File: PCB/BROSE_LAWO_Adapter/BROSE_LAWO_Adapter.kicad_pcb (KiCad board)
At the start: 2 copper layers, 37 x 89.5 mm, 7 parts, among them J1 LAWO Controller, J2 BROSE, J3 24V

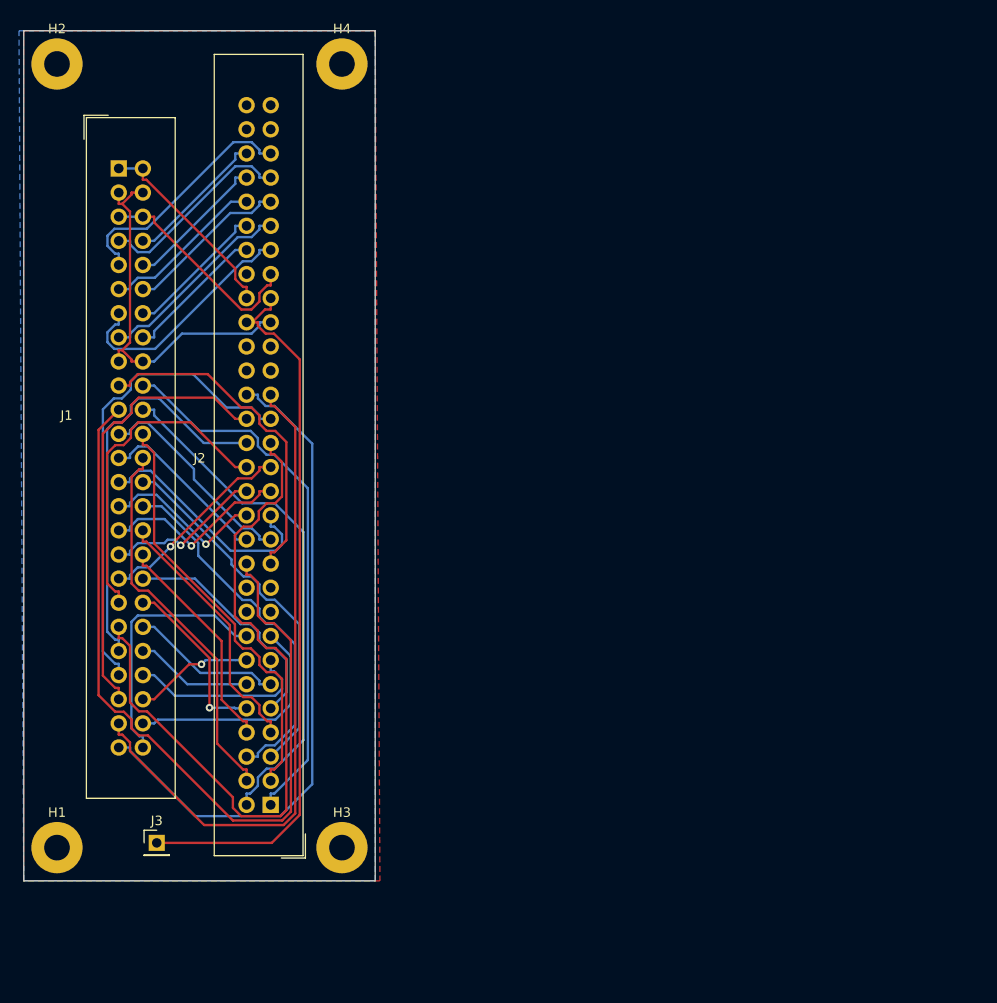
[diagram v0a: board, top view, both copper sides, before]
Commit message: update BROSE_LAWO Adapter PCB
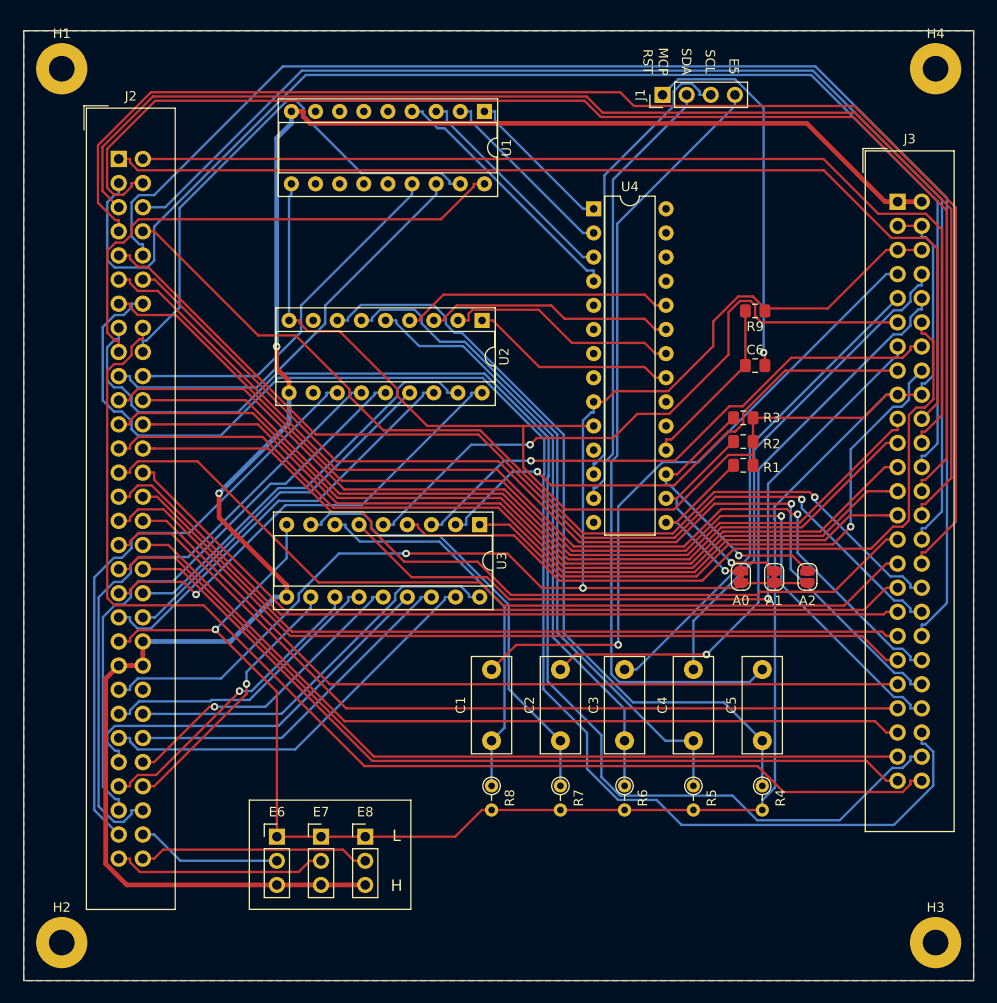
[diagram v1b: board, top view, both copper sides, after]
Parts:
- added C1: 330n, Capacitor_THT:C_Rect_L10.0mm_W4.0mm_P7.50mm_MKS4, F.Cu at (62.2, 87.8)
- added C2: 330n, Capacitor_THT:C_Rect_L10.0mm_W4.0mm_P7.50mm_MKS4, F.Cu at (69.5, 87.8)
- added C3: 330n, Capacitor_THT:C_Rect_L10.0mm_W4.0mm_P7.50mm_MKS4, F.Cu at (76.2, 87.8)
- added C4: 330n, Capacitor_THT:C_Rect_L10.0mm_W4.0mm_P7.50mm_MKS4, F.Cu at (83.5, 87.8)
- added C5: 330n, Capacitor_THT:C_Rect_L10.0mm_W4.0mm_P7.50mm_MKS4, F.Cu at (90.8, 87.8)
- added C6: 100n, Capacitor_SMD:C_0805_2012Metric_Pad1.15x1.40mm_HandSolder, F.Cu at (90.0, 48.2)
- added JP1: E6, Connector_PinHeader_2.54mm:PinHeader_1x03_P2.54mm_Vertical, F.Cu at (39.6, 97.8)
- added JP2: E7, Connector_PinHeader_2.54mm:PinHeader_1x03_P2.54mm_Vertical, F.Cu at (44.3, 97.8)
- added JP3: E8, Connector_PinHeader_2.54mm:PinHeader_1x03_P2.54mm_Vertical, F.Cu at (49.0, 97.8)
- added JP4: A0, Jumper:SolderJumper-2_P1.3mm_Bridged_RoundedPad1.0x1.5mm, F.Cu at (88.5, 70.5)
- added JP5: A1, Jumper:SolderJumper-2_P1.3mm_Bridged_RoundedPad1.0x1.5mm, F.Cu at (92.0, 70.5)
- added JP6: A2, Jumper:SolderJumper-2_P1.3mm_Open_RoundedPad1.0x1.5mm, F.Cu at (95.5, 70.5)
- added R1: 10k, Resistor_SMD:R_0805_2012Metric_Pad1.15x1.40mm_HandSolder, F.Cu at (88.8, 58.8)
- added R2: 10k, Resistor_SMD:R_0805_2012Metric_Pad1.15x1.40mm_HandSolder, F.Cu at (88.8, 56.2)
- added R3: 10k, Resistor_SMD:R_0805_2012Metric_Pad1.15x1.40mm_HandSolder, F.Cu at (88.8, 53.8)
- added R4: 15k, Resistor_THT:R_Axial_DIN0204_L3.6mm_D1.6mm_P2.54mm_Vertical, F.Cu at (90.8, 92.5)
- added R5: 15k, Resistor_THT:R_Axial_DIN0204_L3.6mm_D1.6mm_P2.54mm_Vertical, F.Cu at (83.5, 92.5)
- added R6: 15k, Resistor_THT:R_Axial_DIN0204_L3.6mm_D1.6mm_P2.54mm_Vertical, F.Cu at (76.2, 92.5)
- added R7: 15k, Resistor_THT:R_Axial_DIN0204_L3.6mm_D1.6mm_P2.54mm_Vertical, F.Cu at (69.5, 92.5)
- added R8: 15k, Resistor_THT:R_Axial_DIN0204_L3.6mm_D1.6mm_P2.54mm_Vertical, F.Cu at (62.2, 92.5)
- added R9: 10k, Resistor_SMD:R_0805_2012Metric_Pad1.15x1.40mm_HandSolder, F.Cu at (90.0, 42.5)
- added U1: UDN2981A / TBD62783, Package_DIP:DIP-18_W7.62mm_Socket, F.Cu at (61.5, 21.5)
- added U2: ULN2803A, Package_DIP:DIP-18_W7.62mm_Socket, F.Cu at (61.2, 43.5)
- added U3: ULN2803A, Package_DIP:DIP-18_W7.62mm_Socket, F.Cu at (61.0, 65.0)
- added U4: MCP23017_SP, Package_DIP:DIP-28_W7.62mm, F.Cu at (73.0, 31.8)
- J1: value LAWO Controller -> Conn_01x04; footprint Connector_IDC:IDC-Header_2x25_P2.54mm_Vertical -> Connector_PinHeader_2.54mm:PinHeader_1x04_P2.54mm_Vertical
- J3: value 24V -> LAWO Controller; footprint Connector_PinHeader_2.54mm:PinHeader_1x01_P2.54mm_Vertical -> Connector_IDC:IDC-Header_2x25_P2.54mm_Vertical
- moved J3 103.2 mm to (105.0, 31.0)
- moved H2 92.5 mm to (17.0, 109.0)
- moved H1 82.0 mm to (17.0, 17.0)
- moved J2 69.9 mm to (23.0, 26.5), turned to 0 degrees
- moved H3 63.3 mm to (109.0, 109.0)
- moved H4 62.5 mm to (109.0, 17.0)
- moved J1 57.8 mm to (80.2, 19.8), turned to 90 degrees
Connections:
- J1 pad 1: /VS -> /MCP_RESET
- J1 pad 2: /VS -> /SDA
- J1 pad 3: GND -> /SCL
- J1 pad 4: GND -> /E5
- J2 pad 17: Net-(J2-Pad17) -> /Y_R17
- J2 pad 18: Net-(J2-Pad18) -> /Y_R18
- J2 pad 19: Net-(J2-Pad19) -> /Y_R19
- J2 pad 20: Net-(J2-Pad20) -> /Y_R20
- J2 pad 37: Net-(J2-Pad37) -> /B_R17
- J2 pad 38: Net-(J2-Pad38) -> /B_R18
- J2 pad 39: Net-(J2-Pad39) -> /B_R19
- J2 pad 40: Net-(J2-Pad40) -> /B_R20
- J2 pad 42: Net-(J2-Pad42) -> /VS
- J2 pad 43: Net-(J2-Pad42) -> /VS
- J2 pad 47: /D -> /HV_D
- J2 pad 48: /COL_A0 -> /HV_COL_A0
- J2 pad 49: /COL_A1 -> /HV_COL_A1
- J2 pad 50: /COL_A2 -> /HV_COL_A2
- J2 pad 51: /COL_A3 -> /HV_COL_A3
- J2 pad 52: /COL_A4 -> /HV_COL_A4
- J2 pad 53: /E1 -> /HV_E1
- J2 pad 54: /E2 -> /HV_E2
- J2 pad 55: /E3 -> /HV_E3
- J2 pad 56: /E4 -> /HV_E4
- J2 pad 57: Net-(J2-Pad57) -> /HV_E5
- J2 pad 58: Net-(J2-Pad58) -> /HV_E6
- J2 pad 59: Net-(J2-Pad59) -> /HV_E7
- J2 pad 60: Net-(J2-Pad60) -> /HV_E8
- J3 pad 1: Net-(J2-Pad42) -> /VS
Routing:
- net GND: track 40.2 -> 282.2 mm, vias 0 -> 1
- net /VS: track 21.2 -> 200.8 mm, vias 0 -> 2
- net /Y_R14: track 12.6 -> 150.4 mm, vias 1 -> 0
- net /Y_R10: track 18.6 -> 151.2 mm, vias 1 -> 0
- net +5V: track 23.2 -> 145.0 mm, vias 0 -> 2
- net /Y_R7: track 27.8 -> 147.0 mm
- net /Y_R15: track 24.5 -> 135.8 mm
- net /Y_R5: track 38.7 -> 137.3 mm
- net /Y_R16: track 27.2 -> 125.7 mm
- net /Y_R3: track 44.6 -> 141.5 mm
- net /Y_R12: track 12.4 -> 107.3 mm, vias 0 -> 1
- net /Y_R4: track 40.5 -> 135.0 mm
- net /Y_R6: track 38.5 -> 132.6 mm
- net /Y_R11: track 16.2 -> 107.2 mm, vias 0 -> 1
- net /Y_R13: track 19.6 -> 109.9 mm, vias 0 -> 1
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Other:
- board size 37 x 89.5 mm -> 100 x 100 mm
- board text added: "E5"
- board text added: "H"
- board text added: "L"
- board text added: "MCP RST"
- board text added: "SCL"
- board text added: "SDA"

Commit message: update
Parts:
- removed the J1 at (80.2, 19.8)
- added J2: LAWO Controller 20p, Connector_IDC:IDC-Header_2x10_P2.54mm_Vertical, F.Cu at (104.9, 51.1)
- added U5: 4049, Package_DIP:DIP-16_W7.62mm_Socket, F.Cu at (63.0, 68.3)
- added U6: 4049, Package_DIP:DIP-16_W7.62mm_Socket, F.Cu at (78.0, 65.5)
- H1, H2, H3, H4: footprint MountingHole:MountingHole_2.7mm_Pad -> Connect:1pin
- U4: footprint Package_DIP:DIP-28_W7.62mm -> Package_DIP:DIP-28_W7.62mm_Socket
- moved R9 46.8 mm to (108.2, 85.6), turned to 270 degrees
- moved C6 40.1 mm to (104.6, 85.6), turned to 90 degrees
- moved JP6 31.6 mm to (66.5, 57.9)
- moved JP5 25.3 mm to (70.0, 57.9)
- moved JP4 19.4 mm to (73.7, 57.9)
- moved C1 17.2 mm to (52.6, 102.0)
- moved C2 17.2 mm to (59.8, 102.0)
- moved C3 17.2 mm to (66.6, 102.0)
- moved C4 17.2 mm to (73.8, 102.0)
- moved C5 17.2 mm to (81.1, 102.0)
- moved R4 17.2 mm to (81.1, 106.7)
- moved R5 17.2 mm to (73.8, 106.7)
- moved R6 17.2 mm to (66.6, 106.7)
- moved R7 17.2 mm to (59.8, 106.7)
- moved R8 17.2 mm to (52.6, 106.7)
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- renumbered J3 to J1, J2 to J3
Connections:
- C1 pad 2: /E1 -> Net-(C1-Pad2)
- C2 pad 2: /E2 -> Net-(C2-Pad2)
- C3 pad 2: /E3 -> Net-(C3-Pad2)
- C4 pad 2: /E4 -> Net-(C4-Pad2)
- C5 pad 2: /E5 -> Net-(C5-Pad2)
- U3 pad 1: /COL_A0 -> Net-(U3-Pad1)
- U3 pad 2: /COL_A1 -> Net-(U3-Pad2)
- U3 pad 3: /COL_A2 -> Net-(U3-Pad3)
- U3 pad 4: /COL_A3 -> Net-(U3-Pad4)
- U3 pad 5: /COL_A4 -> Net-(U3-Pad5)
- U3 pad 6: /D -> Net-(U3-Pad6)
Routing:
- net +5V: track 145.0 -> 210.3 mm
- net /Y_R9: track 104.6 -> 167.0 mm, vias 1 -> 0
- net /SCL: track 48.9 -> 102.0 mm
- net Net-(C6-Pad1): track 18.5 -> 69.1 mm
- net /E5: track 83.2 -> 32.6 mm
- net /Y_R4: track 135.0 -> 86.5 mm, vias 0 -> 1
- net /SDA: track 46.7 -> 94.9 mm
- net /Y_R11: track 107.2 -> 152.2 mm, vias 1 -> 0
- net /Y_R6: track 132.6 -> 90.0 mm, vias 0 -> 1
- net /Y_R8: track 102.0 -> 143.7 mm
- net /D: track 78.8 -> 38.5 mm
- net Net-(C1-Pad2): track 0.00 -> 38.3 mm, vias 0 -> 1
- net /VS: track 200.8 -> 163.1 mm, vias 2 -> 0
- net /E1: track 68.5 -> 37.5 mm, vias 1 -> 0
- net Net-(C2-Pad2): track 0.00 -> 29.8 mm
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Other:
- board text removed: "E5"
- board text removed: "MCP RST"
- board text removed: "SCL"
- board text removed: "SDA"

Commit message: update
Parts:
- moved C6 5.00 mm to (104.6, 90.6)
- moved J2 5.00 mm to (104.9, 56.1)
- moved R9 5.00 mm to (108.2, 90.6)
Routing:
- net /Y_R10: track 175.8 -> 105.3 mm, vias 0 -> 1
- net /Y_R12: track 115.9 -> 163.1 mm, vias 2 -> 0
- net /Y_R8: track 143.7 -> 99.3 mm
- net /SCL: track 102.0 -> 59.9 mm, vias 0 -> 1
- net /Y_R4: track 86.5 -> 123.8 mm, vias 1 -> 0
- net /B_R14: track 115.0 -> 79.0 mm, vias 1 -> 0
- net /SDA: track 94.9 -> 61.3 mm, vias 0 -> 1
- net Net-(C5-Pad1): track 100.8 -> 133.4 mm
- net GND: track 283.4 -> 315.6 mm
- net /Y_R15: track 147.1 -> 117.9 mm
- net /Y_R1: track 118.4 -> 91.8 mm
- net /B_R13: track 97.2 -> 123.4 mm
- net Net-(C6-Pad1): track 69.1 -> 94.7 mm, vias 0 -> 1
- net /Y_R16: track 151.5 -> 126.3 mm
- net /Y_R9: track 167.0 -> 142.0 mm
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
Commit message: update pcb
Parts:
- J1: value LAWO Controller -> zum LAWO Controller
- J3: value BROSE -> BROSE Panel
- U4: value MCP23017_SP -> MCP23017
- moved C6 31.4 mm to (104.5, 59.2)
- moved R9 31.4 mm to (108.1, 59.2)
- moved J2 12.7 mm to (104.9, 68.7)
- moved J1 12.4 mm to (93.5, 44.7)
- moved JP3 1.96 mm to (41.9, 98.1)
- moved R4 1.65 mm to (81.1, 105.1)
- moved R5 1.65 mm to (73.8, 105.1)
- moved R6 1.65 mm to (66.6, 105.1)
- moved R7 1.65 mm to (59.8, 105.1)
- moved R8 1.65 mm to (52.6, 105.1)
- moved JP2 0.99 mm to (38.2, 98.1)
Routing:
- net /Y_R8: track 99.3 -> 152.1 mm, vias 1 -> 0
- net Net-(C6-Pad1): track 94.7 -> 43.7 mm, vias 1 -> 0
- net /B_R13: track 123.4 -> 84.9 mm
- net /HV_E1: track 30.1 -> 57.1 mm
- net Net-(C5-Pad1): track 133.4 -> 109.2 mm
- net /HV_E3: track 46.4 -> 69.4 mm
- net /Y_R9: track 142.0 -> 163.1 mm
- net /Y_R15: track 117.9 -> 138.6 mm
- net GND: track 315.6 -> 295.6 mm, vias 12 -> 14
- net /Y_R4: track 123.8 -> 105.3 mm, vias 0 -> 1
- net /Y_R5: track 118.5 -> 100.0 mm, vias 0 -> 1
- net /Y_R1: track 91.8 -> 110.2 mm, vias 0 -> 1
- net /B_R20: track 30.0 -> 48.2 mm, vias 1 -> 0
- net /SCL: track 59.9 -> 76.2 mm, vias 1 -> 0
- net /SDA: track 61.3 -> 76.1 mm, vias 1 -> 0
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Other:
- board text added: "E1"
- board text added: "E5"
- board text added: "UDN2981A / TBD62783"
- board text added: "ULN2803A"
